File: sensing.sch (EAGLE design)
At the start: 78 parts, among them K1 691111710003, U1 TL064ACD, U2 TL431CDBZR, U3 TL431CDBZR, U4 TL431CDBZR, U5 TL431CDBZR, U6 TL431CDBZR, U7 +12v, U8 TL064ACD

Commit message: 1st draft of Vltg sensing part
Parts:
- added C17, C18: 100pF, rcl:C-EUC0402K
- added R39, R40: 30k, rcl:R-EU_M1206
- R31, R32, R33, R34, R35, R36, R37, R38: value 22k -> 1M
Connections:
- net N$22 renamed IC2_PIN5
- net N$23 renamed IC2_PIN6
- net N$24 renamed IC2_PIN10
- net N$25 renamed IC2_PIN9
- net N$26 renamed IC2_PIN12
- net N$27 renamed IC2_PIN13
- net N$30 renamed IC2_PIN7
- net N$31 renamed IC2_PIN8
- net N$32 renamed IC2_PIN14
- removed net N$28: U8.VCC-
- removed net N$29: U8.1OUT
- new net IC2_PIN1: C18.2, R40.2, U8.1OUT
- new net IC2_PIN2: C18.1, R38.2, R40.1, U8.1IN-
- new net IC2_PIN3: C17.2, R34.2, R39.1, U8.1IN+
- new net N$22: R37.2, R38.1
- new net N$23: R35.2, R37.1
- new net N$24: R35.1, R36.2
- new net N$25: K1.3, R32.1
- new net N$26: K1.1, R36.1
- net GND: now also C17.1, R39.2
- net N$1: now also R33.2, R34.1; no longer U8.VCC+
- net N$15: now also R31.2, R33.1; no longer U8.1IN-
- net N$21: now also R31.1, R32.2; no longer U8.1IN+
- net VCC_12+: now also U8.VCC+
- net VCC_12-: now also U8.VCC-
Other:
- moved on the sheet: U8

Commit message: Vltg ckt DONE.. only resistor value setting remaining..!
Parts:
- added C19, C20, C21, C22, C23, C24: 100pF, rcl:C-EUC0402K
- added K2, K3, K4: 691111710003, Wurth_Elektronik_Electromechanic_Terminal_Blocks_Connectors_rev15d:691111710003
- added R41, R42, R43, R44, R45, R46, R47, R48, R51, R52, R53, R54, R55, R56, R57, R58, R61, R62, R63, R64, R65, R66, R67, R68: 1M, rcl:R-EU_M1206
- added R49, R50, R59, R60, R69, R70: 30k, rcl:R-EU_M1206
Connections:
- new net N$27: R41.2, R43.1
- new net N$28: R41.1, R42.2
- new net N$29: R47.2, R48.1
- new net N$30: R45.2, R47.1
- new net N$31: R45.1, R46.2
- new net N$32: R43.2, R44.1
- new net N$33: K2.3, R42.1
- new net N$34: K2.1, R46.1
- new net N$35: R51.2, R53.1
- new net N$36: R51.1, R52.2
- new net N$37: R57.2, R58.1
- new net N$38: R55.2, R57.1
- new net N$39: R55.1, R56.2
- new net N$40: R53.2, R54.1
- new net N$41: K3.3, R52.1
- new net N$42: K3.1, R56.1
- new net N$43: R61.2, R63.1
- new net N$44: R61.1, R62.2
- new net N$45: R67.2, R68.1
- new net N$46: R65.2, R67.1
- new net N$47: R65.1, R66.2
- new net N$48: R63.2, R64.1
- new net N$49: K4.3, R62.1
- new net N$50: K4.1, R66.1
- net GND: now also C19.1, C21.1, C23.1, R49.2, R59.2, R69.2
- net IC2_PIN10: now also C21.2, R54.2, R59.1
- net IC2_PIN12: now also C23.2, R64.2, R69.1
- net IC2_PIN13: now also C24.1, R68.2, R70.1
- net IC2_PIN14: now also C24.2, R70.2
- net IC2_PIN5: now also C19.2, R44.2, R49.1
- net IC2_PIN6: now also C20.1, R48.2, R50.1
- net IC2_PIN7: now also C20.2, R50.2
- net IC2_PIN8: now also C22.2, R60.2
- net IC2_PIN9: now also C22.1, R58.2, R60.1
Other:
- moved on the sheet: C17, C18, K1, R31, R32, R33, R34, R35, R36, R37, R38, R39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

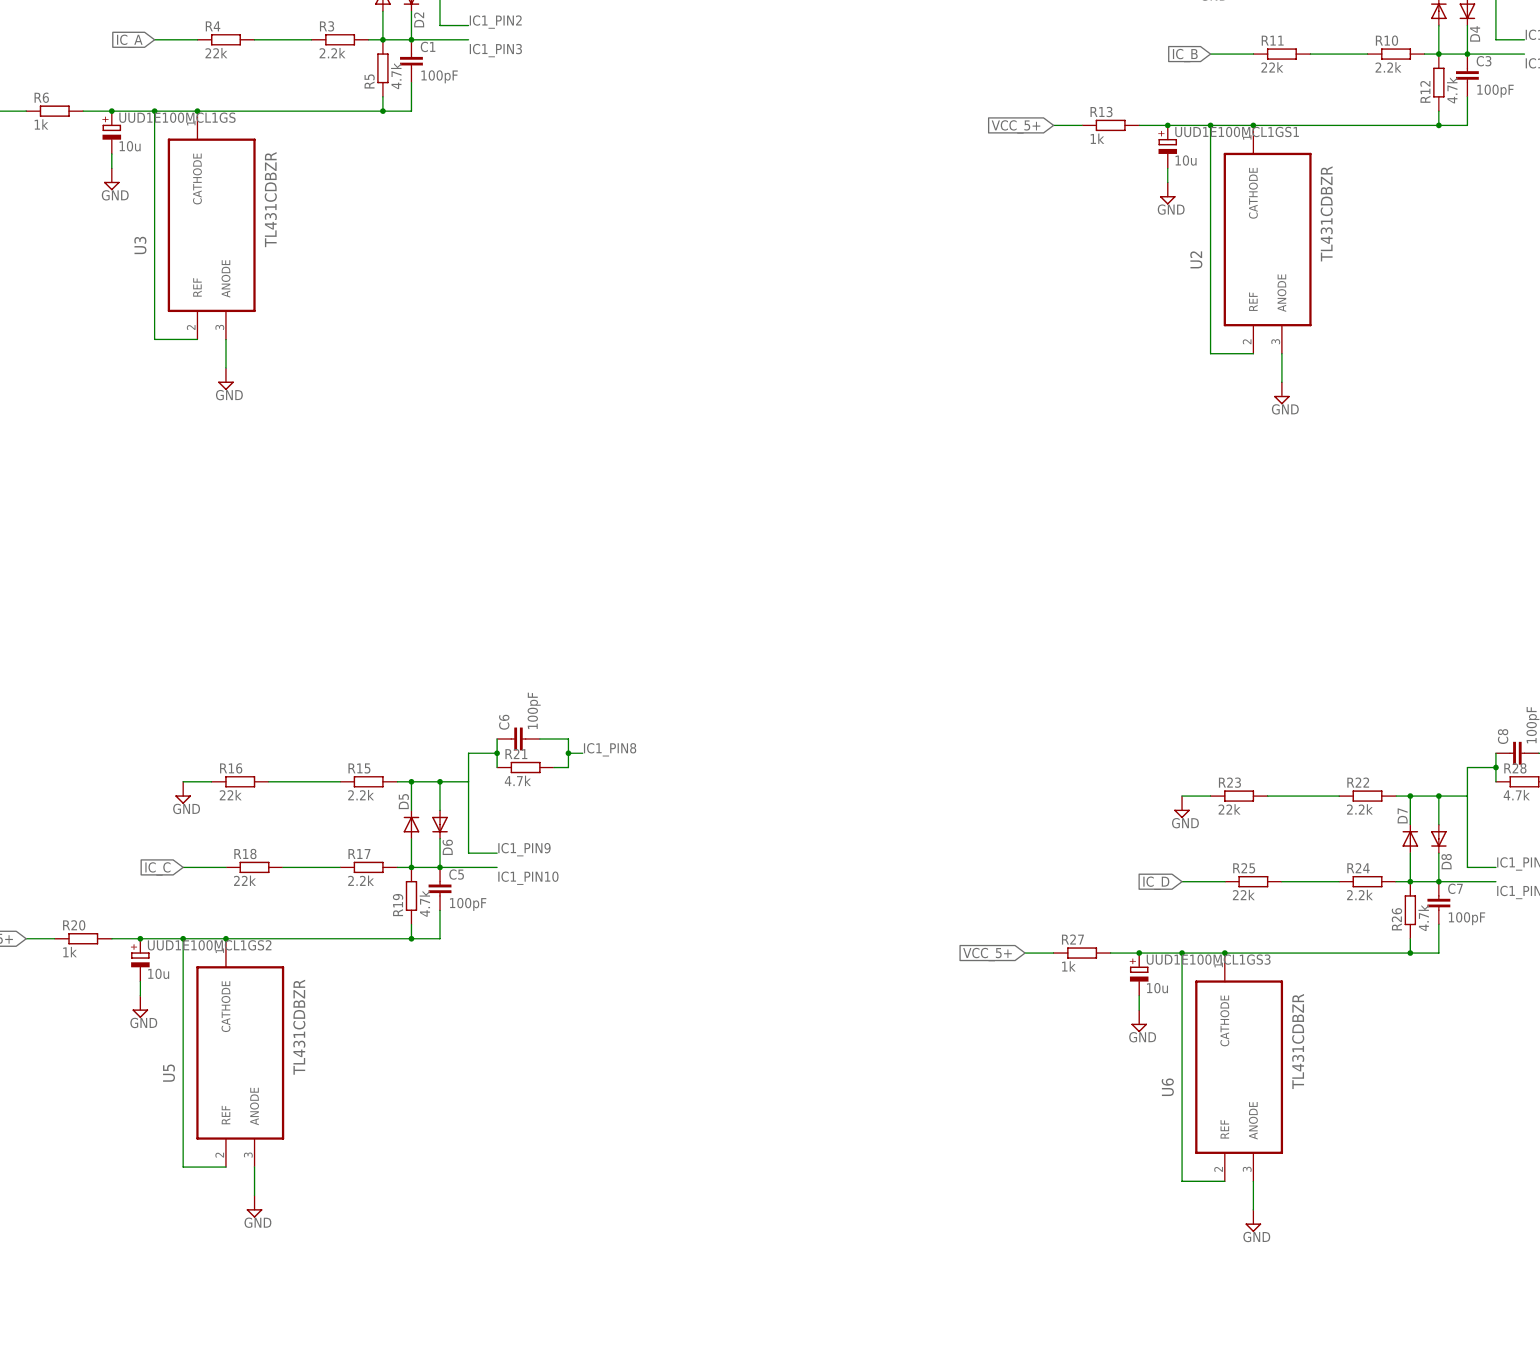
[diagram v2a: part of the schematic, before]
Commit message: Changing SMd package to DIP package
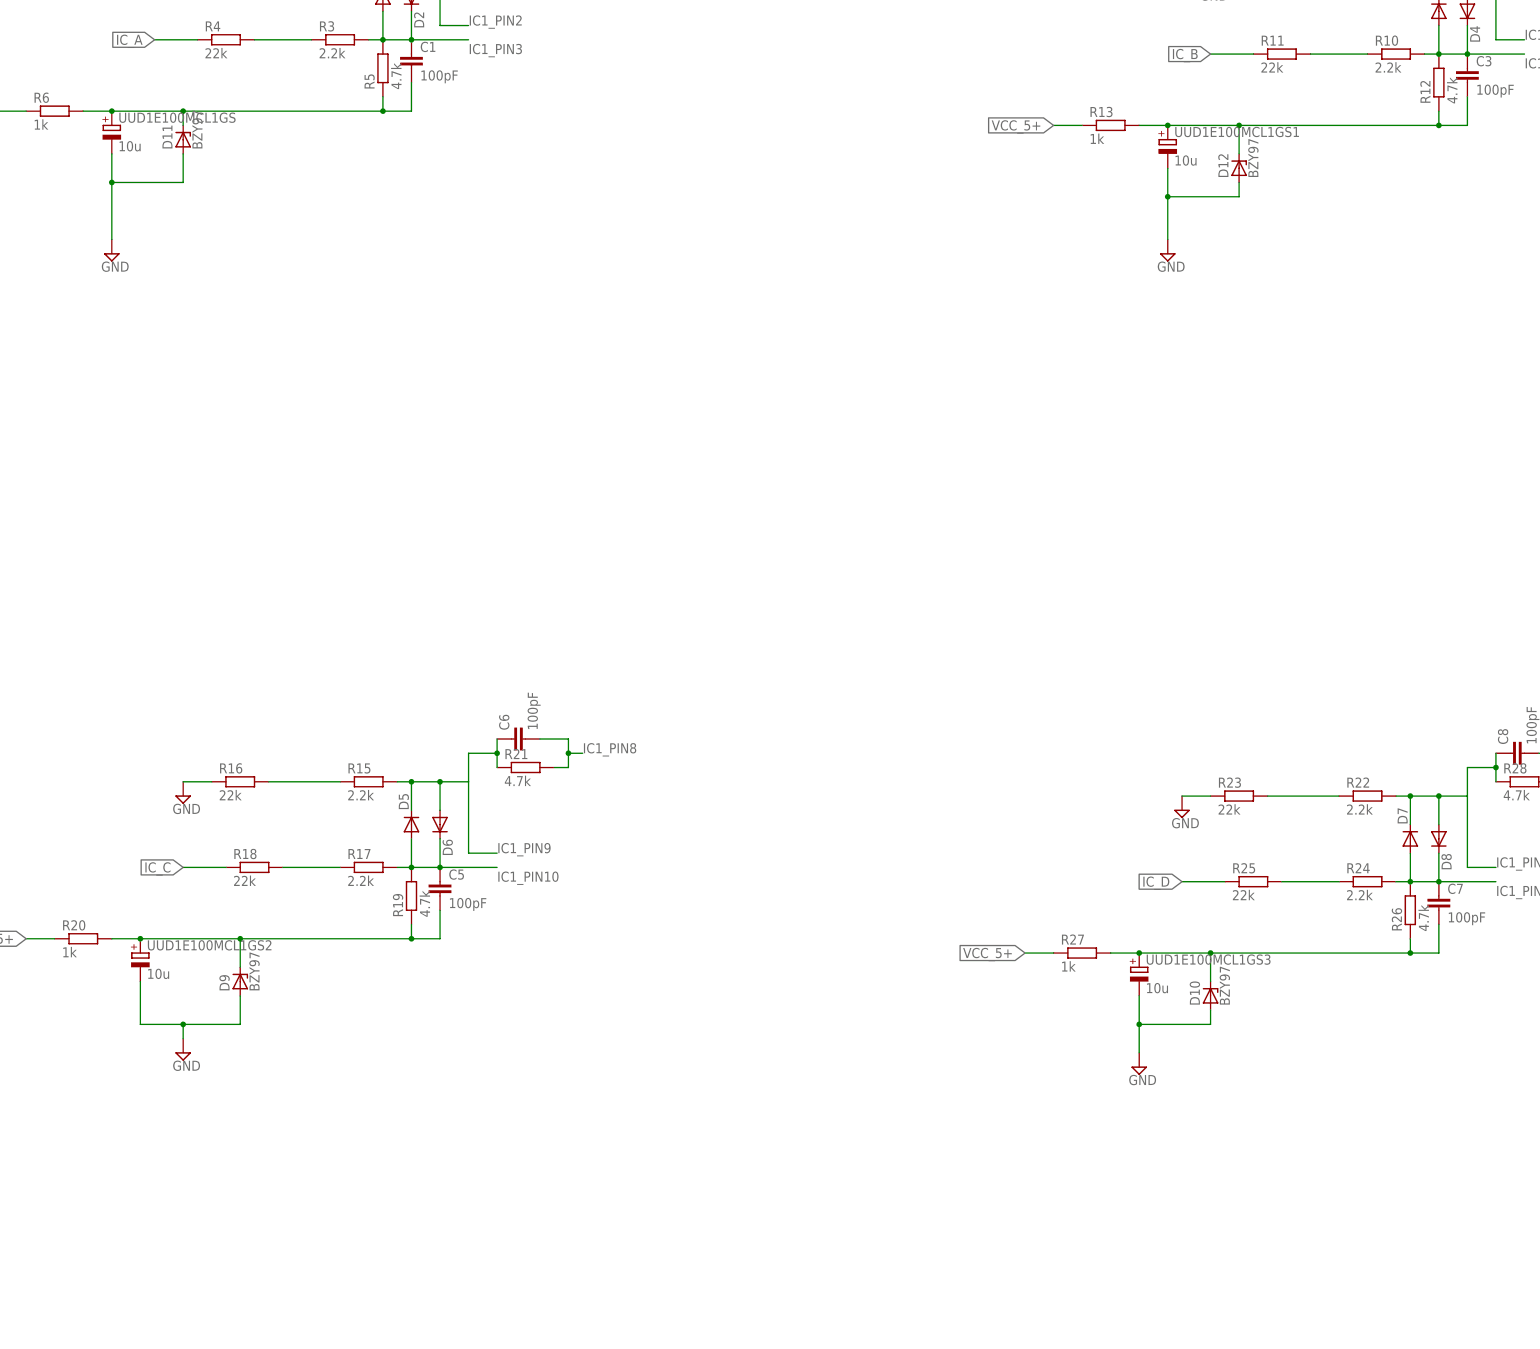
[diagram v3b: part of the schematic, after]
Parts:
- removed U2, U3, U5, U6: TL431CDBZR, Texas Instruments_By_element14_Batch_1:TL431CDBZR
- added D10, D11, D12, D9: BZY97, diode:BZY97
- D1, D2, D3, D4, D5, D6, D7, D8: device diode:DIODE-SOD106-W -> diode:DIODE-DO41-10
- R1, R10, R11, R12, R13, R14, R15, R16, R17, R18, R19, R2, R20, R21, R22, R23, R24, R25, R26, R27, R28, R29, R3, R30, R31, R32, R34, R35, R36, R37, R38, R39, R4, R40, R41, R42, R43, R44, R45, R46, R47, R48, R49, R5, R50, R51, R52, R53, R54, R55, R56, R57, R58, R59, R6, R60, R61, R62, R63, R64, R65, R66, R67, R68, R69, R7, R70, R8, R9: device rcl:R-EU_M1206 -> rcl:R-EU_0207/10
- R33: device rcl:R-EU_M1206 -> rcl:R-EU_0207/12
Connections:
- net GND: now also D10.A, D11.A, D12.A, D9.A; no longer U2.ANODE, U3.ANODE, U5.ANODE, U6.ANODE
- net N$13: now also D12.C; no longer U2.CATHODE, U2.REF
- net N$14: now also D10.C; no longer U6.CATHODE, U6.REF
- net N$6: now also D11.C; no longer U3.CATHODE, U3.REF
- net N$9: now also D9.C; no longer U5.CATHODE, U5.REF
